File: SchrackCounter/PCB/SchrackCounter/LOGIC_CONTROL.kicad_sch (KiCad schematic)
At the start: 8 parts, among them U2 LDD080BUE-101A, U3 LTD080BUE-103A, U4 LDD080BUE-101A, U5 MAX7219, U8 DC56-11CGKWA

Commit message: fixes to be made
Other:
- note added: "COMMON CATHODE PINOUT MAY BE WRONG"
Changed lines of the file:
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@@
+		)
+	)
+	(text "COMMON CATHODE\nPINOUT MAY BE WRONG"
+		(exclude_from_sim no)
+		(at 81.28 77.47 0)
+		(effects
+			(font
+				(size 1.27 1.27)
+				(color 255 0 0 1)
+			)
 		)
 	)

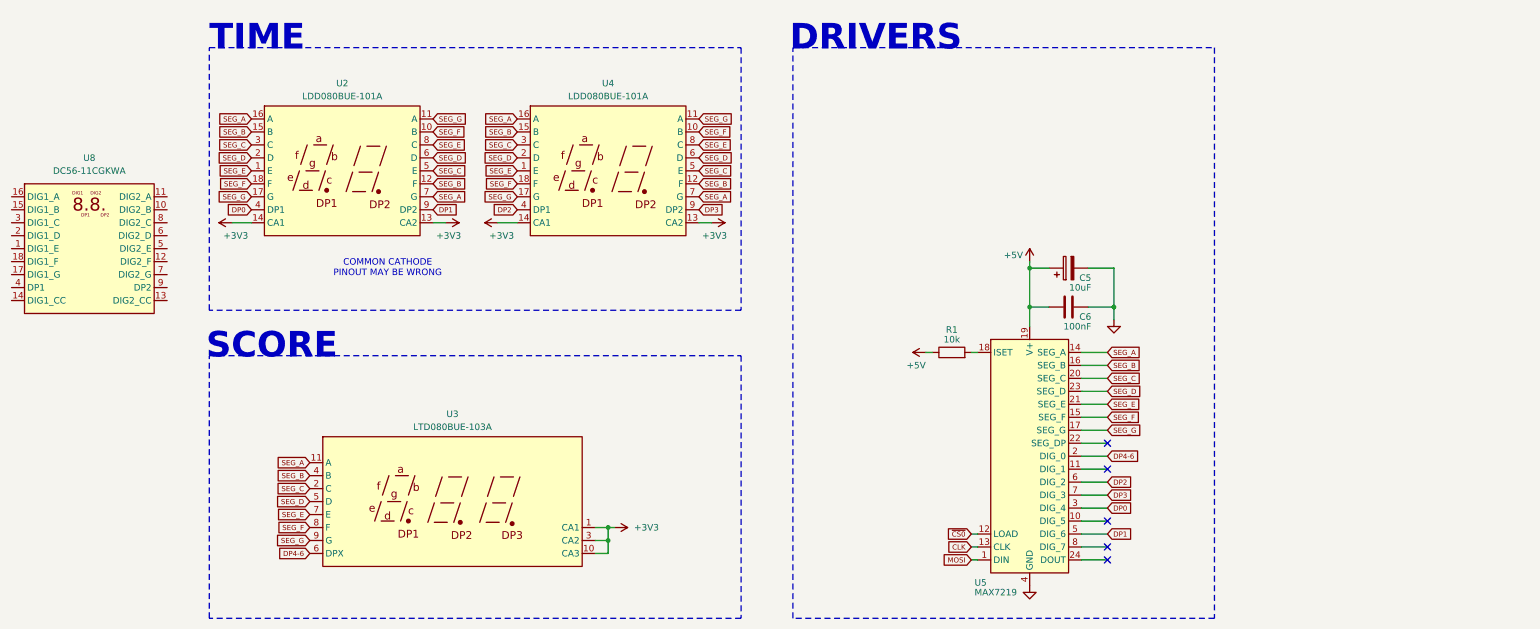
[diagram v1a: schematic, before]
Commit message: PCB and Schematic updates
Fixed 7seg footprints, common cathode, fixed pinout.

PCB razed and started from scratch
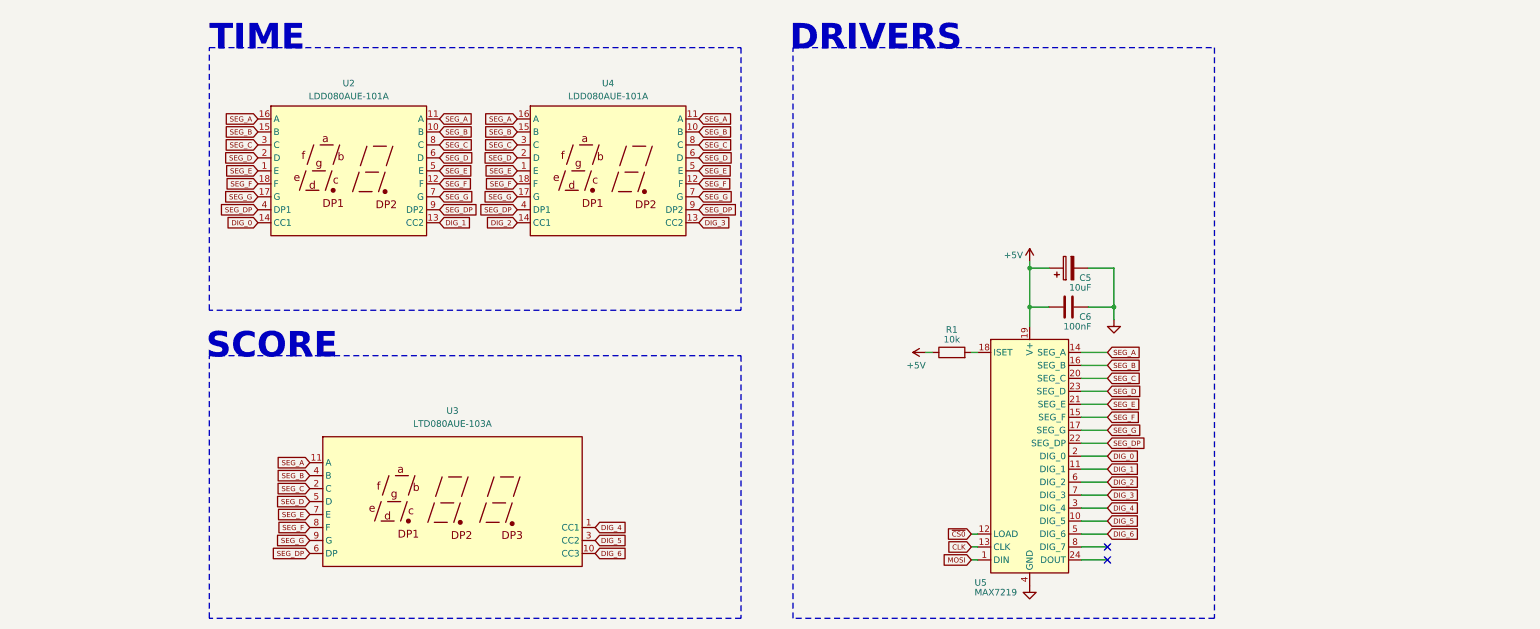
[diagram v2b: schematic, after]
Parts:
- removed U2, U4: LDD080BUE-101A, Schrack_brd:LDD080BUE-101A_made_by_bismarx, symbol SchrackThingy_library:LDD080BUE-101A_made_by_bismarx
- removed U3: LTD080BUE-103A, Schrack_brd:LTD080BUE-103A_made_by_bismarx, symbol SchrackThingy_library:LTD080BUE-103A_made_by_bismarx
- removed U8: DC56-11CGKWA, Display_7Segment:DA56-11CGKWA, symbol Display_Character:DC56-11CGKWA
- added U2, U4: LDD080AUE-101A, Schrack_brd:WENRUN_LDD080x_7segment_2dig, symbol SchrackThingy_library:LDD080AUE-101A
- added U3: LTD080AUE-103A, Schrack_brd:WENRUN_LTD080x_7segment_3dig, symbol SchrackThingy_library:LTD080AUE-103A
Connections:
- net SEG_A: now also U2.11 (A), U2.16 (A), U3.11 (A), U4.11 (A), U4.16 (A)
- net SEG_B: now also U2.10 (B), U2.15 (B), U3.4 (B), U4.10 (B), U4.15 (B)
- net SEG_C: now also U2.3 (C), U2.8 (C), U3.2 (C), U4.3 (C), U4.8 (C)
- net SEG_D: now also U2.2 (D), U2.6 (D), U3.5 (D), U4.2 (D), U4.6 (D)
- net SEG_E: now also U2.1 (E), U2.5 (E), U3.7 (E), U4.1 (E), U4.5 (E)
- net SEG_F: now also U2.12 (F), U2.18 (F), U3.8 (F), U4.12 (F), U4.18 (F)
- net SEG_G: now also U2.17 (G), U2.7 (G), U3.9 (G), U4.17 (G), U4.7 (G)
- net DIG_5: now reaches U5.10 (DIG_5)
- net DIG_5: now also U3.3 (CC2)
- net DIG_1: now reaches U5.11 (DIG_1)
- net DIG_1: now also U2.13 (CC2)
- net SEG_DP: now reaches U5.22 (SEG_DP)
- net SEG_DP: now also U2.4 (DP1), U2.9 (DP2), U3.6 (DP), U4.4 (DP1), U4.9 (DP2)
- net DP0 renamed DIG_4
- net DIG_4: now also U3.1 (CC1)
- net DP1 renamed DIG_6
- net DIG_6: now also U3.10 (CC3)
- net DP2 renamed DIG_2
- net DIG_2: now also U4.14 (CC1)
- net DP3 renamed DIG_3
- net DIG_3: now also U4.13 (CC2)
- net DP4-6 renamed DIG_0
- net DIG_0: now also U2.14 (CC1)
- no-connect marks 5 -> 2
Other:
- note removed: "COMMON CATHODE PINOUT MAY BE WRONG"

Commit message: PCB update
pcb redesign
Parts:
- U5: footprint Package_DIP:DIP-24_W10.16mm -> Package_SO:SOP-24_7.5x15.4mm_P1.27mm
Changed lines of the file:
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@@
 			)
 		)
-		(property "Footprint" "Package_DIP:DIP-24_W10.16mm"
+		(property "Footprint" "Package_SO:SOP-24_7.5x15.4mm_P1.27mm"
 			(at 205.74 113.03 0)
 			(effects

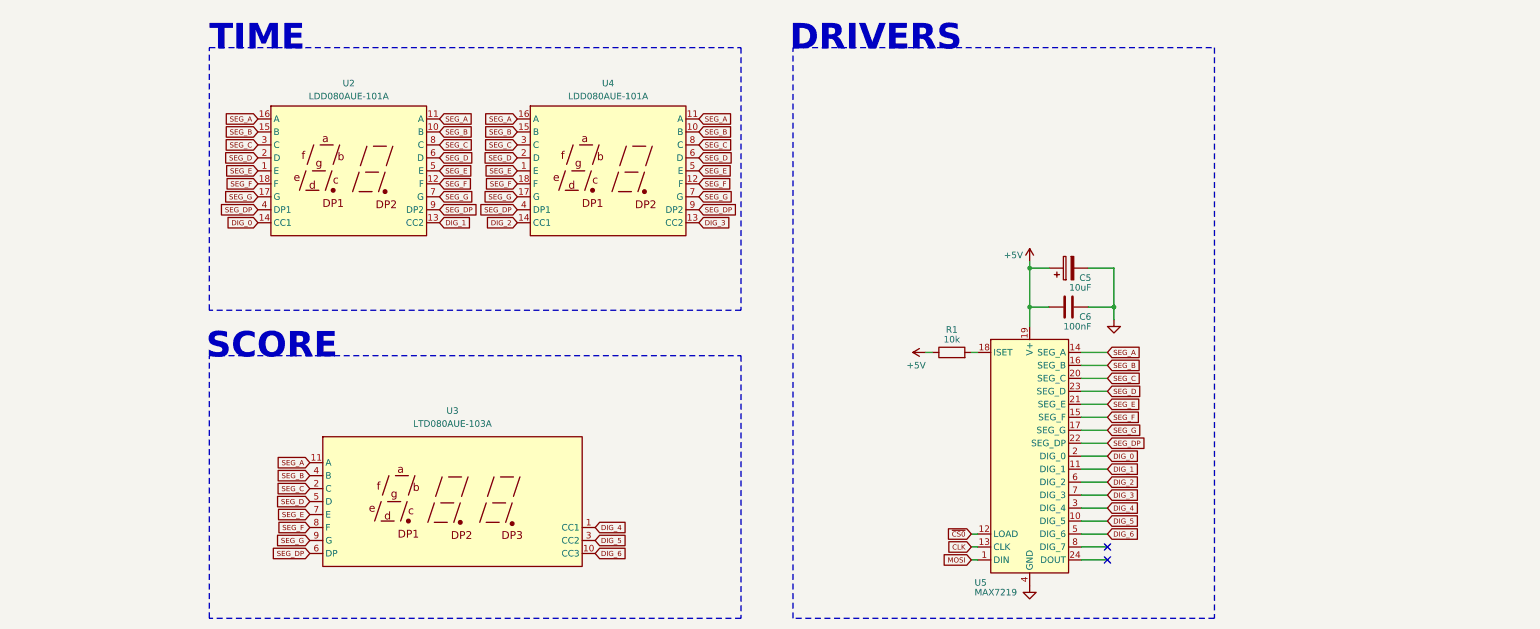
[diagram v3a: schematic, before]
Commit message: PCB LAYOUT UPDATE
Routing, gnd planes
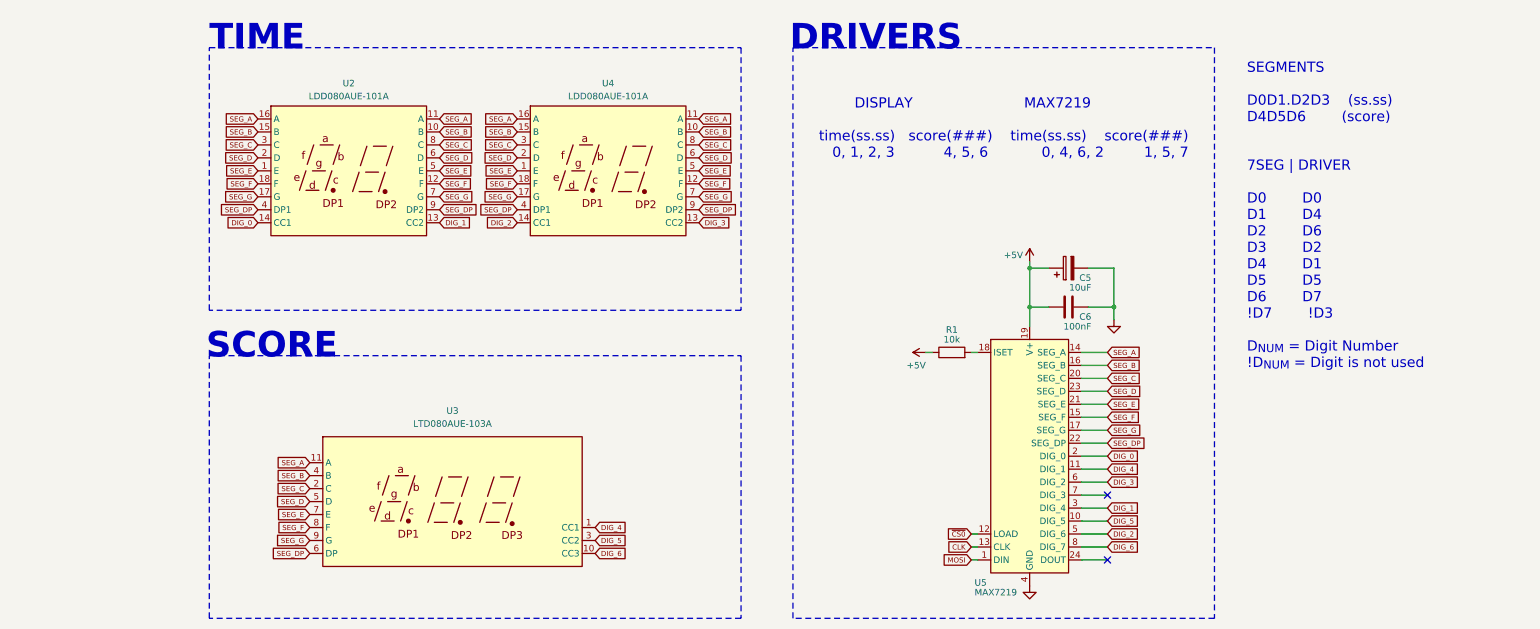
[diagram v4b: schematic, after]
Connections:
- net DIG_1: now also U5.3 (DIG_4); no longer U5.11 (DIG_1)
- net DIG_2: now also U5.5 (DIG_6); no longer U5.6 (DIG_2)
- net DIG_3: now also U5.6 (DIG_2); no longer U5.7 (DIG_3)
- net DIG_4: now also U5.11 (DIG_1); no longer U5.3 (DIG_4)
- net DIG_6: now also U5.8 (DIG_7); no longer U5.5 (DIG_6)
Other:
- note added: "7SEG | DRIVER D0 D0 D1 D4 D2 D6 D3 D2 D4 D1 D5 D5 D6 D7 !D7 !D3 D_{NUM} = Digit Number !D_{NUM} = Digit is not used"
- note added: "DISPLAY MAX7219 time(ss.ss) score(###) time(ss.ss) score(###) 0, 1, 2, 3 4, 5, 6 0, 4, 6, 2 1, 5, 7"
- note added: "SEGMENTS D0D1.D2D3 (ss.ss) D4D5D6 (score)"

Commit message: pcb layput and routong update
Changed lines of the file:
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@@
 	(text "		DISPLAY            			 MAX7219\n\ntime(ss.ss)   score(###)    time(ss.ss)    score(###)\n   0, 1, 2, 3           4, 5, 6            0, 4, 6, 2         1, 5, 7"
 		(exclude_from_sim no)
-		(at 165.735 50.165 0)
+		(at 170.18 47.625 0)
 		(effects
 			(font

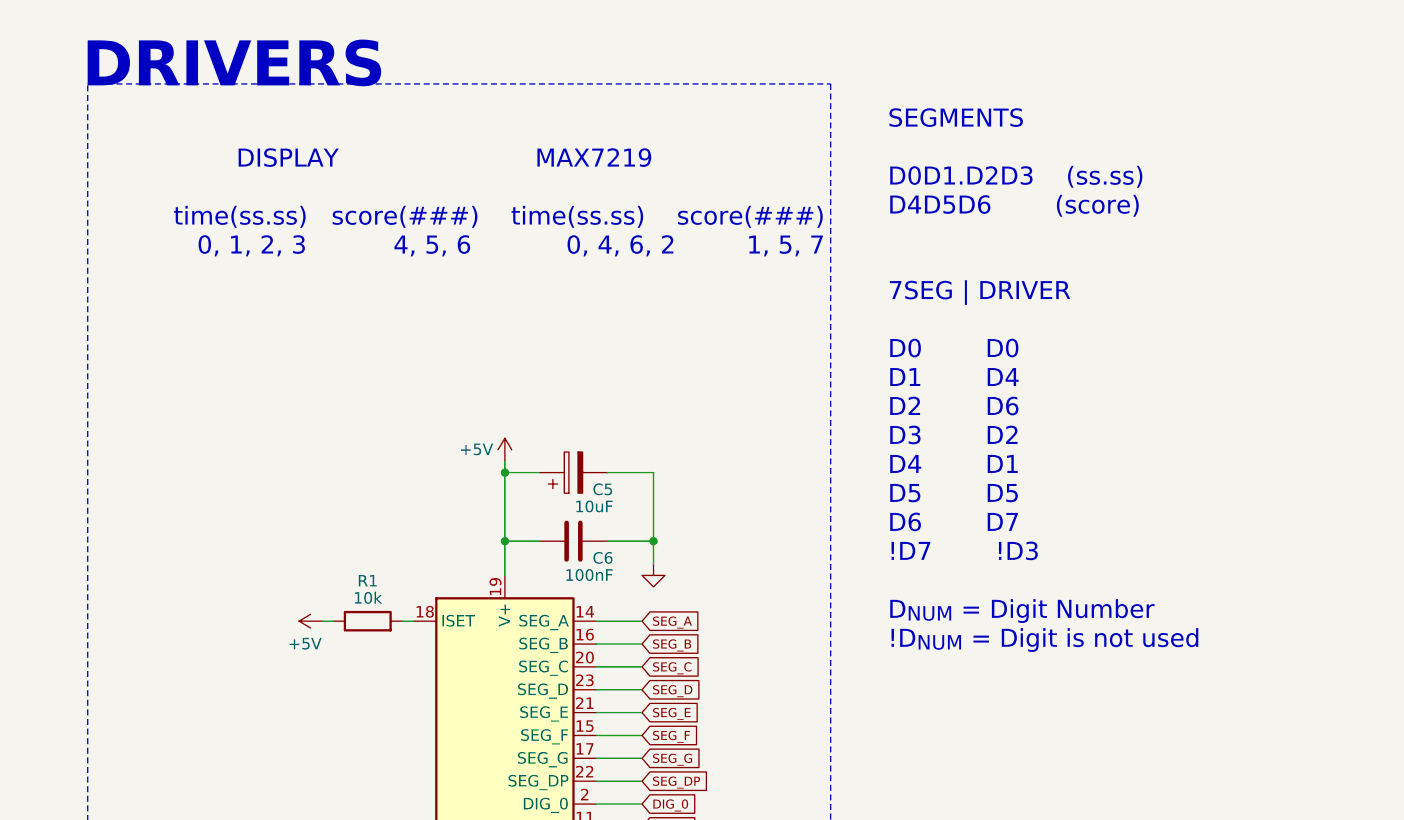
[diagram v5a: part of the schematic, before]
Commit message: SchrackMulticlock and Counter update
Schematic update for both
PCB update for Counter
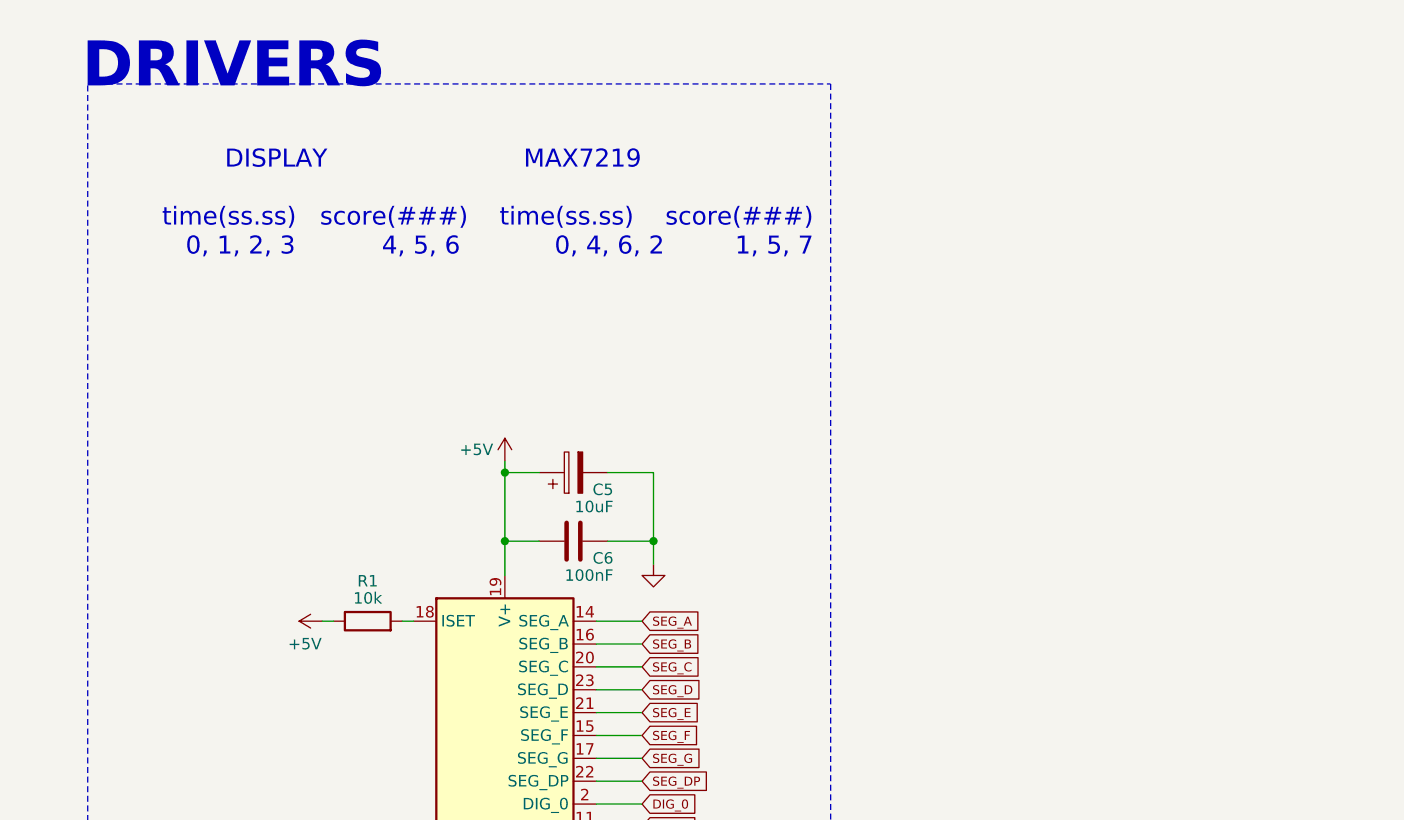
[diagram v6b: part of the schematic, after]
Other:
- note removed: "7SEG | DRIVER D0 D0 D1 D4 D2 D6 D3 D2 D4 D1 D5 D5 D6 D7 !D7 !D3 D_{NUM} = Digit Number !D_{NUM} = Digit is not used"
- note removed: "SEGMENTS D0D1.D2D3 (ss.ss) D4D5D6 (score)"
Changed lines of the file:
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@@
 	(text "		DISPLAY            			 MAX7219\n\ntime(ss.ss)   score(###)    time(ss.ss)    score(###)\n   0, 1, 2, 3           4, 5, 6            0, 4, 6, 2         1, 5, 7"
 		(exclude_from_sim no)
-		(at 170.18 47.625 0)
+		(at 168.91 47.625 0)
 		(effects
 			(font
@@
 		)
 	)
-	(text "7SEG | DRIVER\n\nD0		D0\nD1		D4\nD2		D6\nD3		D2\nD4		D1\nD5		D5\nD6		D7\n!D7		!D3\n\nD_{NUM} = Digit Number\n!D_{NUM} = Digit is not used\n"
-		(exclude_from_sim no)
-		(at 249.555 76.835 0)
-		(effects
-			(font
-				(face "Bahnschrift")
-				(size 2 2)
-				(color 0 0 0 1)
-			)
-			(justify left)
-		)
-	)
 	(text "TIME"
 		(exclude_from_sim no)
@@
 				(color 0 0 0 1)
 			)
-			(justify left)
-		)
-	)
-	(text "SEGMENTS \n\nD0D1.D2D3    (ss.ss)\nD4D5D6        (score)\n"
-		(exclude_from_sim no)
-		(at 249.555 43.18 0)
-		(effects
-			(font
-				(face "Bahnschrift")
-				(size 2 2)
-				(color 0 0 0 1)
-			)

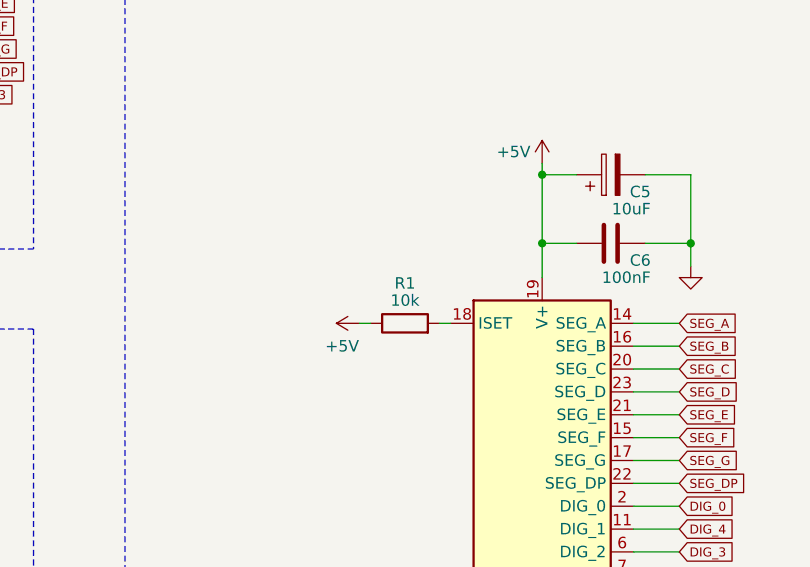
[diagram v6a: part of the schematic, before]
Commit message: SchrackMulticlock and Counter pcb updates
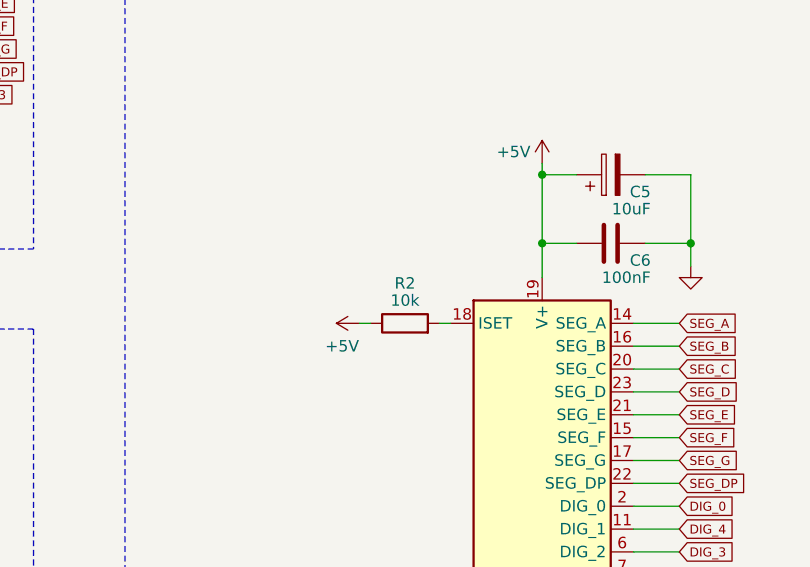
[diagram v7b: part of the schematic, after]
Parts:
- renumbered R1 to R2
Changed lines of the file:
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@@
 		(dnp no)
 		(fields_autoplaced yes)
-		(property "Reference" "#PWR09"
+		(property "Reference" "#PWR011"
 			(at 223.52 93.98 0)
 			(effects
@@
 			(project "SchrackCounter"
 				(path "/d96f2ffc-3f4c-4f71-b693-29f6b8c3245d/50491303-1200-42ed-9e6c-90c20c198c18"
-					(reference "#PWR09")
+					(reference "#PWR011")
 					(unit 1)
 				)
@@
 		(on_board yes)
 		(dnp no)
-		(property "Reference" "#PWR07"
+		(property "Reference" "#PWR09"
 			(at 207.01 80.01 0)
 			(effects
@@
 			(project "SchrackCounter"
 				(path "/d96f2ffc-3f4c-4f71-b693-29f6b8c3245d/50491303-1200-42ed-9e6c-90c20c198c18"
-					(reference "#PWR07")
+					(reference "#PWR09")
 					(unit 1)
 				)
@@
 		(on_board yes)
 		(dnp no)
-		(property "Reference" "R1"
+		(property "Reference" "R2"
 			(at 191.77 89.535 90)
 			(effects
@@
 			(project "SchrackCounter"
 				(path "/d96f2ffc-3f4c-4f71-b693-29f6b8c3245d/50491303-1200-42ed-9e6c-90c20c198c18"
-					(reference "R1")
+					(reference "R2")
 					(unit 1)
 				)
@@
 		(on_board yes)
 		(dnp no)
-		(property "Reference" "#PWR06"
+		(property "Reference" "#PWR08"
 			(at 190.5 93.98 0)
 			(effects
@@
 			(project "SchrackCounter"
 				(path "/d96f2ffc-3f4c-4f71-b693-29f6b8c3245d/50491303-1200-42ed-9e6c-90c20c198c18"
-					(reference "#PWR06")
+					(reference "#PWR08")
 					(unit 1)
 				)
@@
 		(dnp no)
 		(fields_autoplaced yes)
-		(property "Reference" "#PWR08"
+		(property "Reference" "#PWR010"
 			(at 207.01 146.05 0)
 			(effects
@@
 			(project "SchrackCounter"
 				(path "/d96f2ffc-3f4c-4f71-b693-29f6b8c3245d/50491303-1200-42ed-9e6c-90c20c198c18"
-					(reference "#PWR08")
-					(unit 1)
-				)
+					(reference "#PWR010")
+					(unit 1)
+				)
